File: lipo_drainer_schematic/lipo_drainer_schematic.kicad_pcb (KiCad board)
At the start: 2 copper layers, 58 parts, among them J1 BATT, J2 FAN, J3 Vcal, J4 128x64_OLED, J5 Gcal, J6 Ical, J7 Heatsink Temp (for MCP7901), Q1 MMBT3904, Q10 G700P06T, Q11 G700P06T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

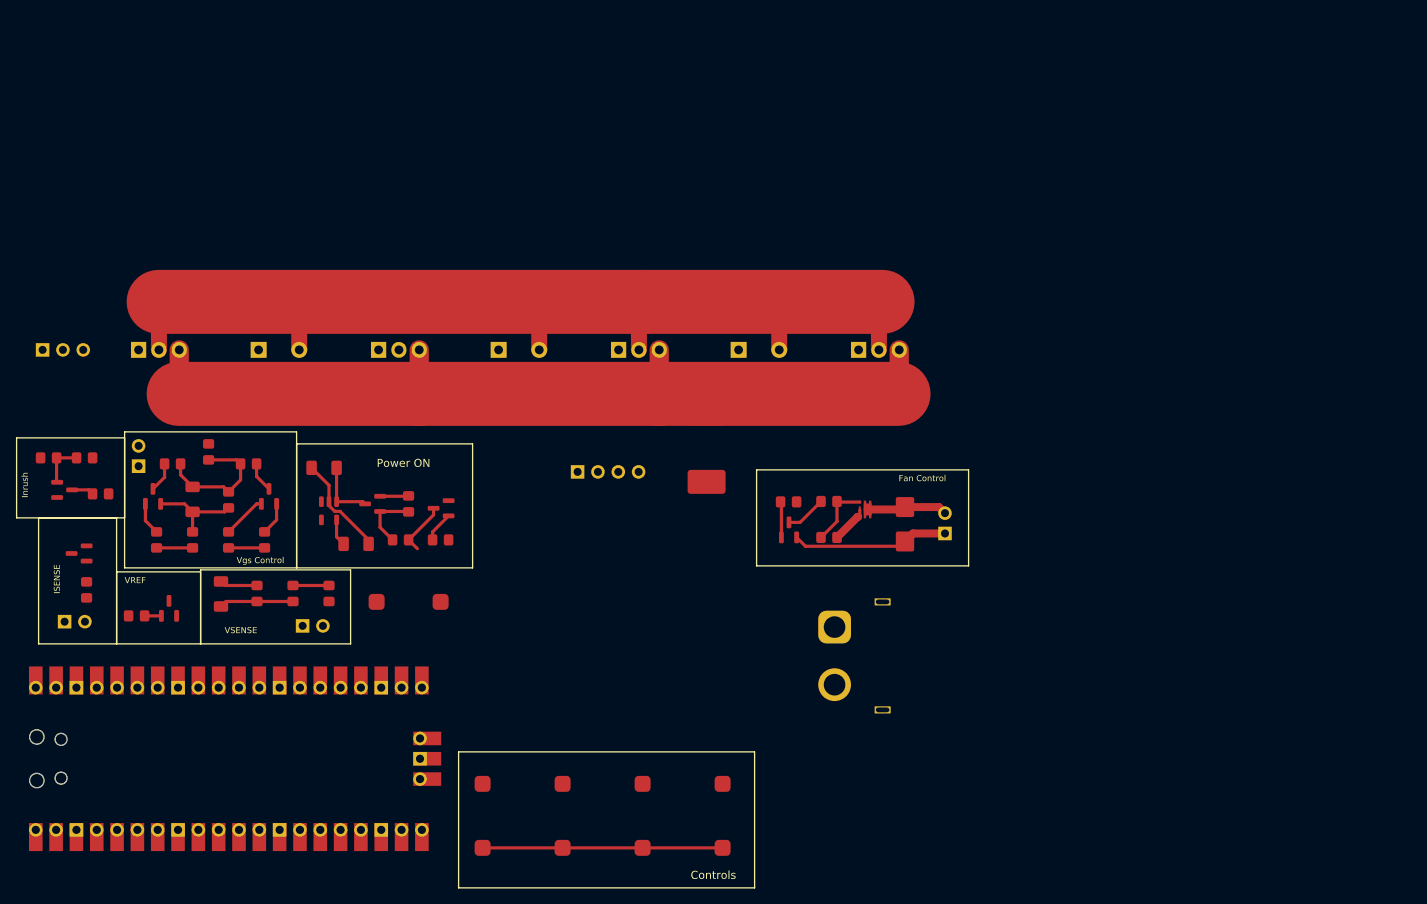
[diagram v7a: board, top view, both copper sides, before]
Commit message: Routed and added mounting holes.
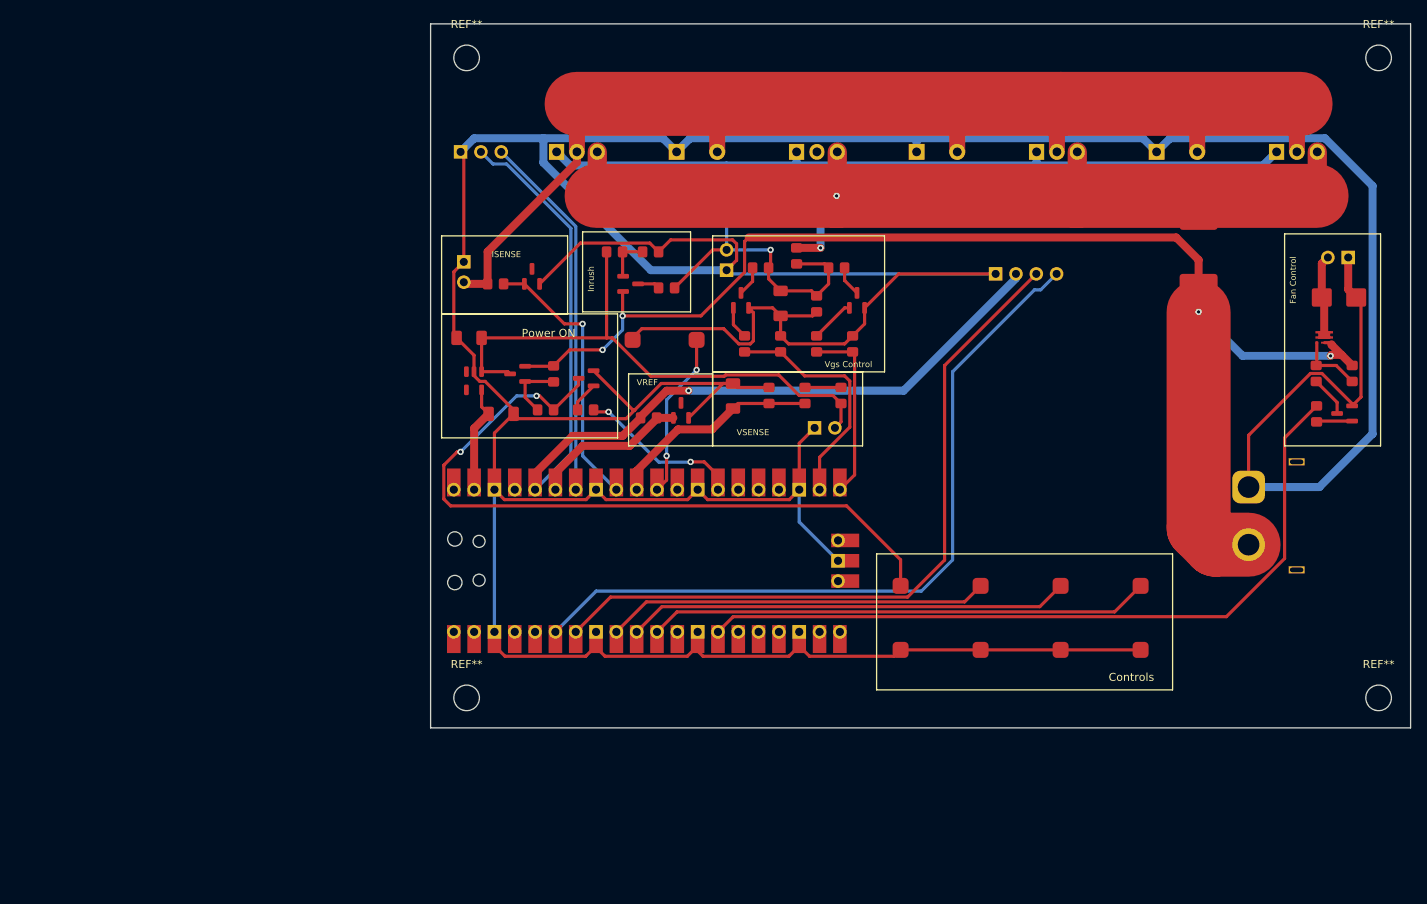
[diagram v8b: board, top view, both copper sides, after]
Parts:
- added REF**: MountingHole_3.2mm_M3, MountingHole:MountingHole_3.2mm_M3, F.Cu at (206.0, 134.0)
- added REF**: MountingHole_3.2mm_M3, MountingHole:MountingHole_3.2mm_M3, F.Cu at (92.0, 54.0)
- added REF**: MountingHole_3.2mm_M3, MountingHole:MountingHole_3.2mm_M3, F.Cu at (206.0, 54.0)
- added REF**: MountingHole_3.2mm_M3, MountingHole:MountingHole_3.2mm_M3, F.Cu at (92.0, 134.0)
- moved Q9 77.5 mm to (140.8, 84.3)
- moved C4 77.5 mm to (131.2, 84.7)
- moved J5 77.5 mm to (124.5, 80.5)
- moved Q6 77.5 mm to (126.3, 84.3)
- moved R14 77.5 mm to (131.2, 89.8)
- moved R15 77.5 mm to (126.8, 89.8)
- moved R16 77.5 mm to (133.2, 78.8)
- moved R17 77.5 mm to (128.8, 80.2)
- moved R18 77.5 mm to (140.2, 89.8)
- moved R19 77.5 mm to (135.8, 89.8)
- moved R20 77.5 mm to (138.2, 80.2)
- moved R25 77.5 mm to (135.8, 84.8)
- moved Q5 75.3 mm to (112.5, 82.2)
- moved R12 75.3 mm to (115.0, 78.2)
- moved R13 75.3 mm to (117.0, 82.8)
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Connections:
- U2 pad 20: /EN -> unconnected-(U2-GPIO15-Pad20)
- U2 pad 27: unconnected-(U2-GPIO21-Pad27) -> /EN
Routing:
- net GND: track 83.0 -> 647.4 mm
- net /BAT+: track 8.27 -> 160.6 mm, vias 0 -> 4
- net /3V3: track 0.00 -> 124.4 mm, vias 0 -> 1
- net /FET-G: track 16.6 -> 138.5 mm, vias 0 -> 1
- net /FAN: track 0.00 -> 95.4 mm
- net /SDA: track 0.00 -> 95.0 mm
- net /SCL: track 0.00 -> 90.3 mm
- net /ON: track 6.80 -> 91.0 mm, vias 0 -> 2
- net /OK: track 0.00 -> 62.8 mm
- net /VHIGH: track 7.90 -> 70.5 mm
- net /NEXT: track 0.00 -> 55.4 mm
- net /OFF: track 0.00 -> 47.9 mm
- net /TEMP: track 0.00 -> 46.1 mm
- net /CUR: track 0.00 -> 34.4 mm, vias 0 -> 1
- net /SLOW: track 4.50 -> 29.8 mm
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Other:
- board outline added: 122.5 x 88 mm
